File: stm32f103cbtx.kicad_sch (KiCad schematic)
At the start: 40 parts, among them J10 Conn_01x02, J11 Conn_01x02, J12 Conn_01x02, J3 693071010811, J4 Conn_01x03, J5 Conn_01x02, J6 Conn_01x05, J7 Conn_01x03, J8 Conn_01x04, Q1 BC817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

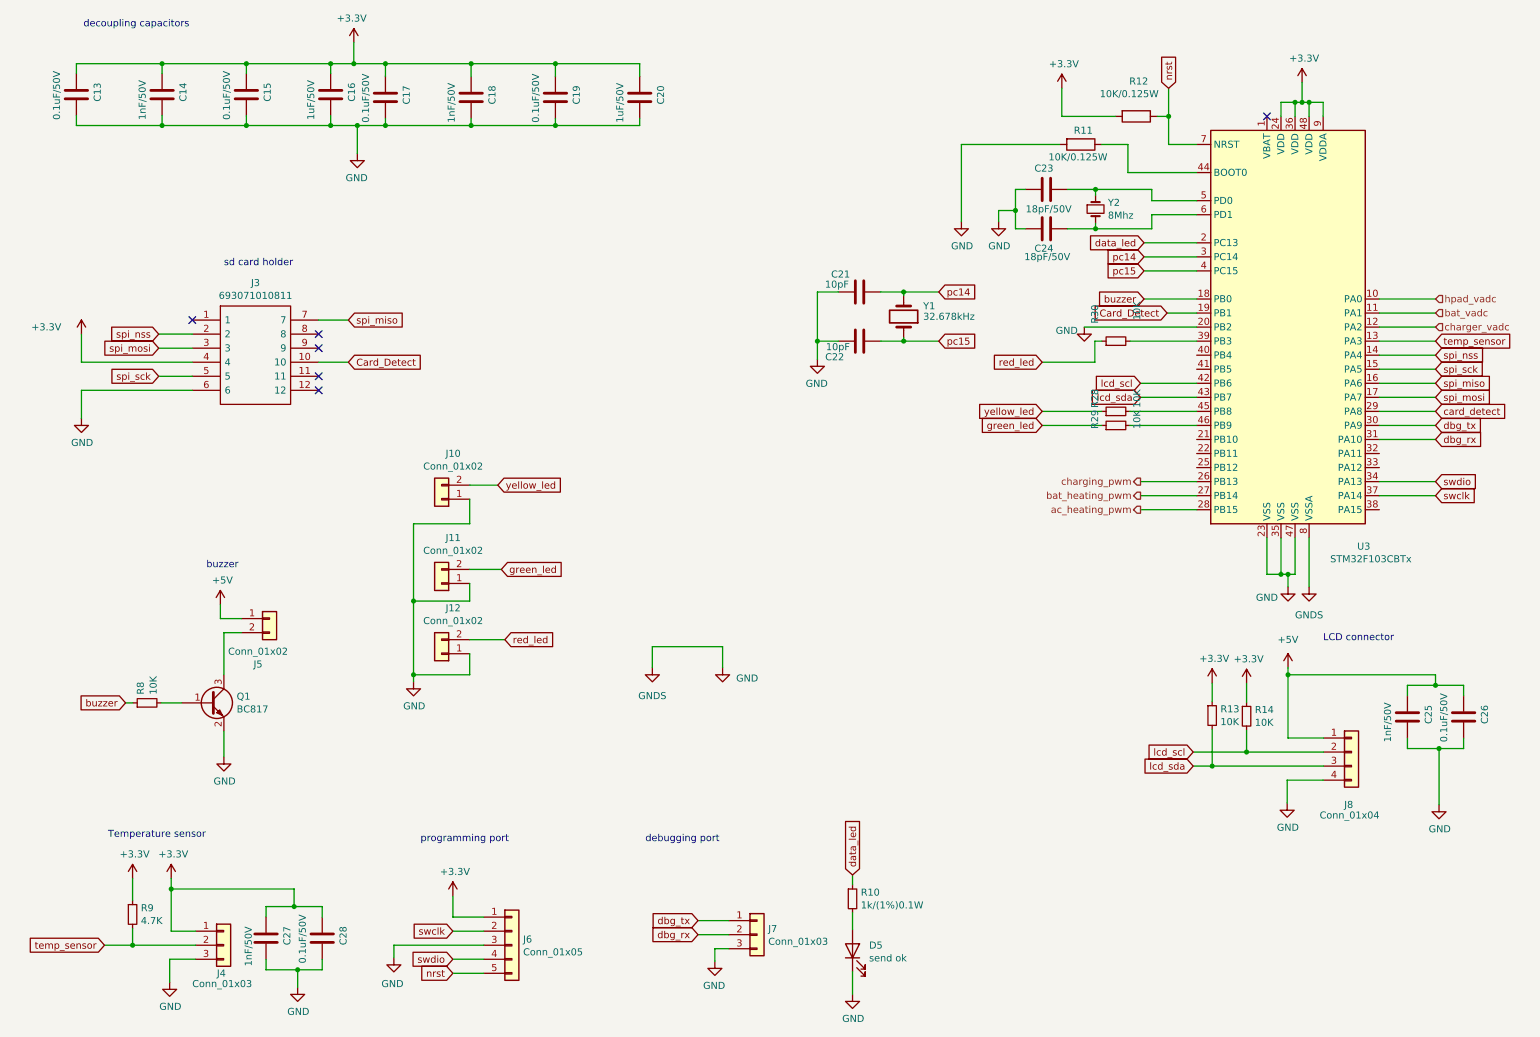
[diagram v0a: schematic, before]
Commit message: Formatted schematic and Increased power tracks
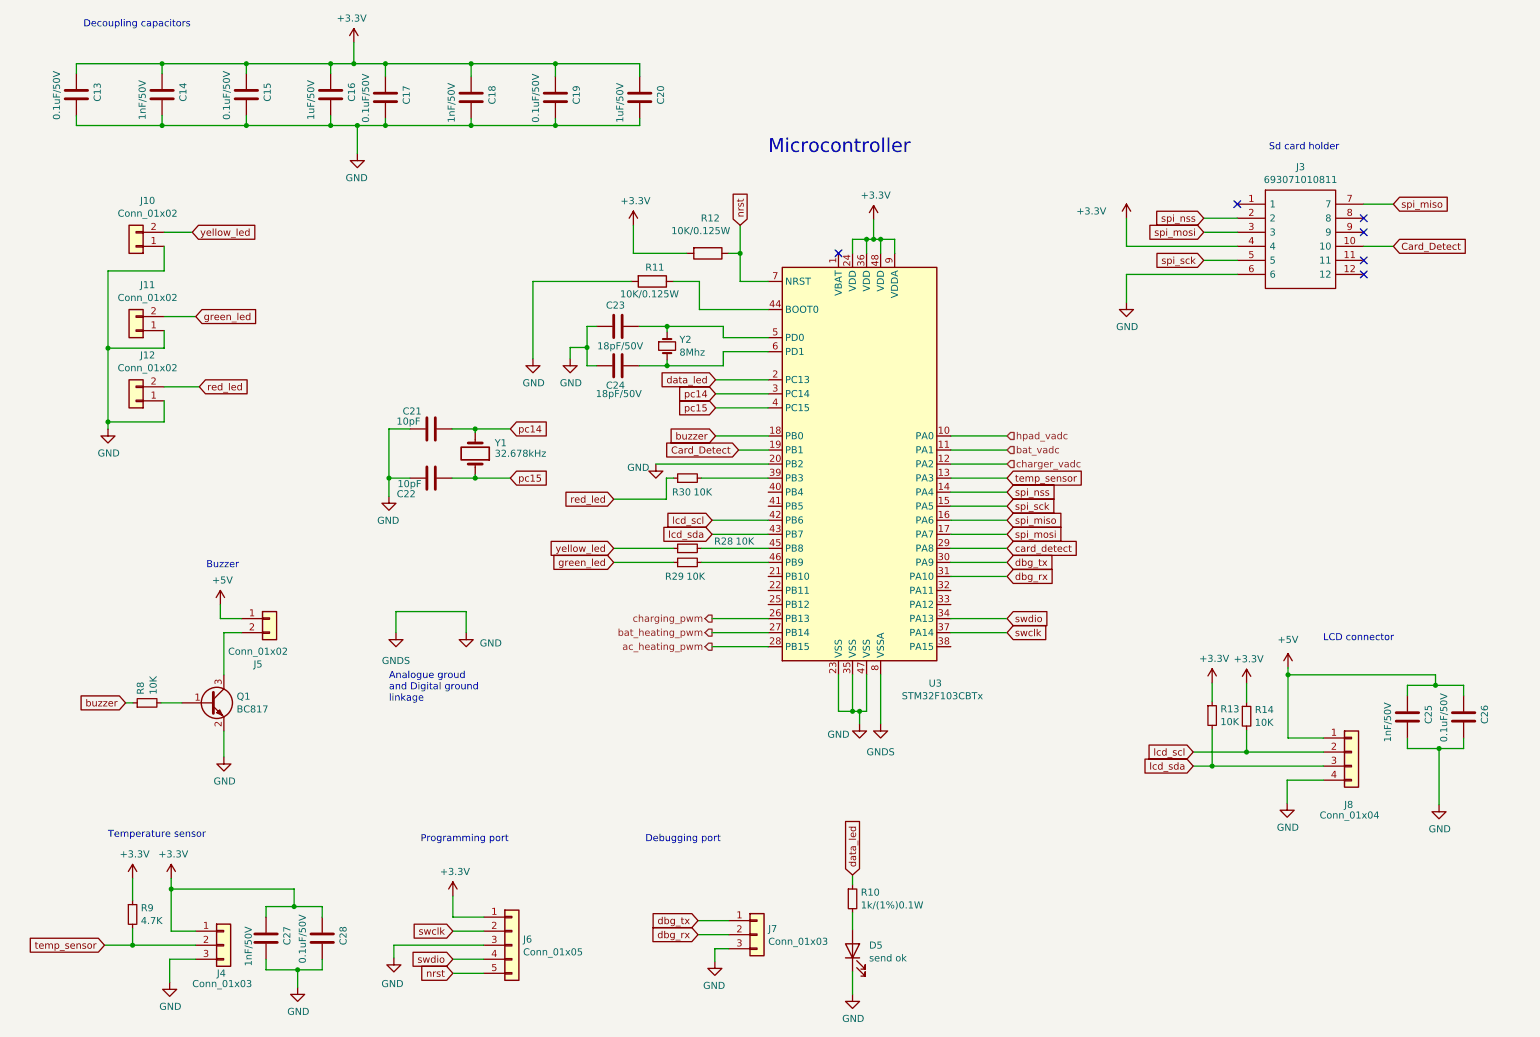
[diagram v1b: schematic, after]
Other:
- note added: "Analogue groud and Digital ground linkage"
- note added: "Buzzer"
- note added: "Debugging port"
- note added: "Decoupling capacitors"
- note added: "Microcontroller"
- note added: "Programming port"
- note added: "Sd card holder"
- note removed: "buzzer"
- note removed: "debugging port"
- note removed: "decoupling capacitors"
- note removed: "programming port"
- note removed: "sd card holder"
- company: (none) -> Che innovations
- title: (none) -> Neonest v 1.3
- moved on the sheet: C21, C22, C23, C24, J10, J11, J12, J3, R11, R12, R28, R29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

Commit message: Minor changes, generated gerber files and submitted
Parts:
- added JP1: Jumper_2_Bridged, Jumper:SolderJumper-2_P1.3mm_Bridged2Bar_RoundedPad1.0x1.5mm, symbol Jumper:Jumper_2_Bridged
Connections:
- net GND: now also JP1.2 (B); no longer U3.8 (VSSA)
- new net GNDS: JP1.1 (A), U3.8 (VSSA)
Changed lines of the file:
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@@
     (stroke (width 0) (type default))
   )
-  (wire (pts (xy 92.71 121.92) (xy 92.71 125.73))
+  (wire (pts (xy 92.71 120.65) (xy 92.71 125.73))
     (stroke (width 0) (type default))
   )
@@
     (stroke (width 0) (type default))
   )
+  (wire (pts (xy 80.01 120.65) (xy 81.28 120.65))
+    (stroke (width 0) (type default))
+  )
   (wire (pts (xy 56.515 186.69) (xy 62.23 186.69))
     (stroke (width 0) (type default))
@@
     (stroke (width 0) (type default))
   )
-  (wire (pts (xy 80.01 125.73) (xy 80.01 121.92))
-    (stroke (width 0) (type default))
-  )
   (wire (pts (xy 226.06 53.34) (xy 232.1306 53.34))
     (stroke (width 0) (type default))
@@
     (stroke (width 0) (type default))
   )
+  (wire (pts (xy 80.01 120.65) (xy 80.01 125.73))
+    (stroke (width 0) (type default))
+  )
   (wire (pts (xy 56.515 184.785) (xy 56.515 186.69))
     (stroke (width 0) (type default))
@@
     (stroke (width 0) (type default))
   )
+  (wire (pts (xy 91.44 120.65) (xy 92.71 120.65))
+    (stroke (width 0) (type default))
+  )
   (wire (pts (xy 232.1306 55.88) (xy 212.09 55.88))
     (stroke (width 0) (type default))
@@
   )
   (wire (pts (xy 267.97 135.255) (xy 262.89 135.255))
-    (stroke (width 0) (type default))
-  )
-  (wire (pts (xy 80.01 121.92) (xy 92.71 121.92))
     (stroke (width 0) (type default))
   )
@@
         )
       )
+    )
+  )
+  (symbol (lib_id "Jumper:Jumper_2_Bridged") (at 86.36 120.65 0) (unit 1)
+    (in_bom yes) (on_board yes) (dnp no) (fields_autoplaced)
+    (property "Reference" "JP1" (at 86.36 115.57 0)
+      (effects (font (size 1.27 1.27)))
+    )
+    (property "Value" "Jumper_2_Bridged" (at 86.36 118.11 0)
+      (effects (font (size 1.27 1.27)))
+    )
+    (property "Footprint" "Jumper:SolderJumper-2_P1.3mm_Bridged2Bar_RoundedPad1.0x1.5mm" (at 86.36 120.65 0)
+      (effects (font (size 1.27 1.27)) hide)
+    )
+    (property "Datasheet" "~" (at 86.36 120.65 0)
+      (effects (font (size 1.27 1.27)) hide)
+    )
+    (pin "2")
+    (pin "1")
+    (instances
+      (project "Neonest_V_1.3"
+        (path "/ce9a6e29-1047-45c4-8057-e81505c21257/0a99568a-0ec0-4b01-8503-a505add38117"
+          (reference "JP1") (unit 1)
+        )
+      )
